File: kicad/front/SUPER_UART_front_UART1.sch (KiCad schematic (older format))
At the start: 46 parts, among them CON1 UART A, CON5 RS232, CON6 UART A, SW16 DTR, SW17 RTS, U1 SN74LVC2T45DCTT, U10 MAX3243EIPW, U13 74HC08N, U14 74HC08N, U2 SN74LVC2T45DCTT

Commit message: Working on schematic
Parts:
- removed C21, C22, C4: 100n, 0603_N, symbol C
- removed C23, C24, C25: 470n, 0603_N, symbol C
- removed CON5: RS232, pnConnector:DB9MV, symbol DB9_MALE
- removed D48: DTR, pnSemiconductor:LED_3.2x2, symbol diode_LED
- removed D49: RTS, pnSemiconductor:LED_3.2x2, symbol diode_LED
- removed MH1, MH2: hole, mounting_hole_3.2_7.5_plated, symbol mounting_hole_plated
- removed R1, R2: R, 0603_R_N, symbol R_V
- removed unit 1 of RN1
- removed RN8: R, 4x0603_N, symbol R_Network_4
- removed SW16: DTR, pnSwitches:TACTB-64K-F, symbol MicroswitchSMT
- removed SW17: RTS, pnSwitches:TACTB-64K-F, symbol MicroswitchSMT
- removed U1, U2: SN74LVC2T45DCTT, niceSemiconductors:TI_SSOP-8_N, symbol SN74LVC2T45DCTT
- removed U10: MAX3243EIPW, TSSOP-28_N, symbol MAX3243EIPW
- removed U13, U14: 74HC08N, DIP-14_N, symbol 74HC08N
- added C13, C26, C28, C31, C34: 100n, 0603_N, symbol C
- added CON4: UART D, pnConnector:NIGINI_NCDW-06, symbol PIN-1x6
- added D21: DTR, pnSemiconductor:LED0603_R, symbol diode_LED
- added D22: CTS, pnSemiconductor:LED0603_R, symbol diode_LED
- added D23: RXD, pnSemiconductor:LED0603_R, symbol diode_LED
- added D24: TXD, pnSemiconductor:LED0603_R, symbol diode_LED
- added D7, D8: PESD5V2S2UT, SOT23-3_N, symbol PESD5V2S2UT
- added Q5, Q6: PDTA143ZT, niceSemiconductors:SOT23-3_N, symbol PDTA143ZT
- added R13, R18: R, 0603_R_N, symbol R_V
- added R14, R15, R16, R17: R, 0603_R_N, symbol R
- added unit 2 of RN1
- added RN3, RN4, RN9: R, pnRLC:4x0603_N, symbol R_network_4
- added T2, T3: DMG1012UW-7, niceSemiconductors:SC70-3_N, symbol N-MOS_small
- added TP6, TP7, TP8, TP9: Testpoint, pnConnector:TP_1mm, symbol Testpoint
- added U1: 74LVC1T45GW, SC70-6_N, symbol 74LVC1T45GW
- added U21, U22: 74LVC8T245PW, TI_TSSOP-24_N, symbol 74LVC8T245PW
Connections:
- net labels added: +3V3, CTS_B, CTS_B_VDDA, CTS_B_VDDB, CTS_D, CTS_D1, CTS_D_VDDA, DCD_D, DCD_D1, DCD_D_VDDA, DSR_D, DSR_D1, DSR_D_VDDA, DTR_B, DTR_B_VDDA, DTR_B_VDDB, DTR_D, DTR_D1, DTR_D_VDDA, I2C_PU_EN_B, I2C_PU_EN_B_VCCA, RI_D, RI_D1, RI_D_VDDA, RTS_D, RTS_D1, RTS_D_VDDA, RXD_B, RXD_B_LED, RXD_B_VDDA, RXD_B_VDDB, RXD_D1, RXD_D_LED, RXD_D_VDDA, TXD_B, TXD_B_LED, TXD_B_VDDA, TXD_B_VDDB, TXD_D, TXD_D_LED, TXD_D_VDDA, VDDA, VDDB, ~CTS_B_OC, ~RXD_B_OC, ~SPI_EN_B
- net labels removed: CTS_A_ISO, CTS_A_LED_ISO, DCD_A_ISO, DCD_A_LED_ISO, DSR_A_ISO, DSR_A_LED_ISO, DTR_A_ISO, DTR_A_LED_ISO, FTDI_DTR_A_ISO, FTDI_DTR_A_ISO1, FTDI_RTS_A_ISO, FTDI_RTS_A_ISO1, FT_CTS_A_ISO, FT_CTS_A_ISO1, FT_CTS_A_ISO2, FT_DCD_A_ISO1, FT_DCD_A_ISO2, FT_DSR_A_ISO1, FT_DSR_A_ISO2, FT_DTR_A_ISO, FT_RI_A_ISO1, FT_RI_A_ISO2, FT_RTS_A_ISO, FT_RXD_A_ISO, FT_RXD_A_ISO1, FT_RXD_A_ISO2, FT_TXD_A_ISO, ISO_3V3, ISO_GND, ISO_VDD, RI_A_ISO, RI_A_LED_ISO, RS_CTS_ISO, RS_DCD_ISO, RS_DSR_ISO, RS_DTR_ISO, RS_RI_ISO, RS_RTS_ISO, RS_RXD_ISO, RS_TXD_ISO, RTS_A_ISO, RTS_A_LED_ISO, RXD_A_ISO, RXD_A_LED, TXD_A_ISO, TXD_A_LED
- wire segments 190 -> 211
- no-connect marks 1 -> 0
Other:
- note added: "Level converter"
- note added: "TTL level connector"
- moved on the sheet: C17, C5, C6, C7, CON1, CON6, D1, D10, D11, D12, D2, D25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

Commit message: Working on schematic
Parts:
- removed D12: CTS, pnSemiconductor:LED0603_R, symbol diode_LED
- removed D29: DSR, pnSemiconductor:LED0603_R, symbol diode_LED
- removed D31: RI, pnSemiconductor:LED0603_R, symbol diode_LED
- removed D32: DCD, pnSemiconductor:LED0603_R, symbol diode_LED
- removed R7: R, 0603_R_N, symbol R
- removed RN4: R, pnRLC:4x0603_N, symbol R_network_4
- removed T2, T3: DMG1012UW-7, niceSemiconductors:SC70-3_N, symbol N-MOS_small
- removed TP6, TP7, TP8, TP9: Testpoint, pnConnector:TP_1mm, symbol Testpoint
- added C26, C32: 100n, 0603_N, symbol C
- added C27: 10n, 0603_N, symbol C
- added C28: 10u, niceRLC:0805_N, symbol C
- added C31: 1u, niceRLC:0603_N, symbol C
- added Q3, Q5: 2N7002PS, niceSemiconductors:SC70-6_N, symbol 2N7002PS
- added Q6: N-MOS_small, SOT23-3_N, symbol N-MOS_small
- added R14: R, 0603_R_N, symbol R
- added R15, R18, R19, R21, R22, R26: 10k, 0603_R_N, symbol R_V
- added R20: 4k7, 0603_R_N, symbol R_V
- added R23: 1k8, 0603_R_N, symbol R_V
- added R24: 3k9, 0603_R_N, symbol R_V
- added R25: 6k8, 0603_R_N, symbol R_V
- added R27: 5k6, 0603_R_N, symbol R
- added R28: 47k, 0603_R_N, symbol R
- added U10: LP2951CD, SOIC-8_N, symbol LP2951CD
- LED29: renamed from D9; Fieldname (none) -> Value
- renumbered C17 to C19, C28 to C20, C5 to C21, C34 to C22, C13 to C23, C31 to C24, C26 to C25, C6 to C29, C7 to C30, CON6 to CON4, CON1 to CON5, CON4 to CON6, D25 to D2, D26 to D3, D27 to D4, D28 to D5, D1 to D6, D2 to D7, D7 to D8, D8 to D9, D11 to LED27, D10 to LED28, D30 to LED30, D21 to LED31, D22 to LED32, D23 to LED33, D24 to LED34, Q5 to Q2, Q6 to Q4, R13 to R10, R15 to R11, R16 to R12, R8 to R13, R18 to R16, R9 to R7, R10 to R8, R14 to R9, RN1 to RN4, RN9 to RN5, RN3 to RN6, U21 to U7, U22 to U8, U1 to U9
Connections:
- net labels added: +5V, CTS_B_VDD1, CTS_D_VDD1, DCD_D_VDD1, DSR_D_VDD1, DTR_B_VDD1, DTR_D_VDD1, RI_D_VDD1, RTS_D_VDD1, RXD_B_VDD1, RXD_D_VDD1, SPI_EN_B, TXD_B_VDD1, TXD_D_VDD1, VDD1, VDD1_SEL1, VDD1_SEL2, VDD1_SEL3, ~VDD1_EN, ~VDD1_ERR
- net labels removed: CTS_B_VDDA, CTS_B_VDDB, CTS_D, CTS_D_VDDA, DCD_D, DCD_D_VDDA, DSR_D, DSR_D_VDDA, DTR_B_VDDA, DTR_B_VDDB, DTR_D, DTR_D_VDDA, RI_D, RI_D_VDDA, RTS_D, RTS_D_VDDA, RXD_B_VDDA, RXD_B_VDDB, RXD_D_VDDA, TXD_B_VDDA, TXD_B_VDDB, TXD_D_VDDA, VDDA, VDDB, ~SPI_EN_B
- wire segments 211 -> 241
- no-connect marks 0 -> 6
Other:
- note removed: "Level converter"
- note removed: "TTL level connector"
- moved on the sheet: C19, C20, C21, C22, C23, C24, C25, C29, C30, CON4, CON5, CON6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

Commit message: Working on schematic
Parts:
- CON4, CON5: value UART A -> PORT D
- CON6: value UART D -> PORT B
- LED27, LED28, LED29, LED30, LED31, LED32, LED33, LED34: footprint pnSemiconductor:LED0603_R -> pnSemiconductor:0805D

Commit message: PCB placement
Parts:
- removed Q3: 2N7002PS, niceSemiconductors:SC70-6_N, symbol 2N7002PS
- added Q3, Q8: N-MOS_small, SOT23-3_N, symbol N-MOS_small
- RN4, RN5, RN6: footprint pnRLC:4x0603_N -> niceRLC:4x0603_N
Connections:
- net CTS_B_VDD1: now also Q8.3 (D)
- net CTS_D_VDD1: now also RN5.3; no longer RN5.2
- net DCD_D_VDD1: now also RN5.2; no longer RN5.3
- net DSR_D_VDD1: now also RN5.1; no longer RN5.4
- net DTR_D_VDD1: now also RN4.3; no longer RN4.2
- net GND: now also Q3.2 (S), Q8.2 (S)
- net RTS_D_VDD1: now also RN4.2; no longer RN4.3
- net RXD_B_VDD1: now also Q3.3 (D)
- net RXD_D_VDD1: now also RN5.4; no longer RN5.1
- net TXD_B_VDD1: now also RN4.1; no longer RN4.4
- net TXD_D_VDD1: now also RN4.4; no longer RN4.1
- net VDD1_SEL1: now also Q6.1 (G); no longer Q5.1 (G)
- net VDD1_SEL3: now also Q5.1 (G); no longer Q6.1 (G)
- net ~CTS_B_OC: now also Q8.1 (G)
- net ~RXD_B_OC: now also Q3.1 (G)
- net at RN4.8: now also U7.18 (B4); no longer U7.21 (B1)
- net at RN4.5: now also U7.21 (B1); no longer U7.18 (B4)
- net at U7.19 (B3): now also RN4.7; no longer RN4.6
- net at U7.20 (B2): now also RN4.6; no longer RN4.7
- net at U8.18 (B4): now also RN5.8; no longer RN5.5
- net at U8.19 (B3): now also RN5.7; no longer RN5.6
- net at U8.20 (B2): now also RN5.6; no longer RN5.7
- net at U8.21 (B1): now also RN5.5; no longer RN5.8
- net at C32.1, R23.1, R28.2: now also Q6.3 (D); no longer Q5.6 (D)
- net at R25.1: now also Q5.6 (D); no longer Q6.3 (D)
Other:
- moved on the sheet: Q5A, Q6, RN4A, RN4B, RN4C, RN4D, RN5A, RN5B, RN5C, RN5D

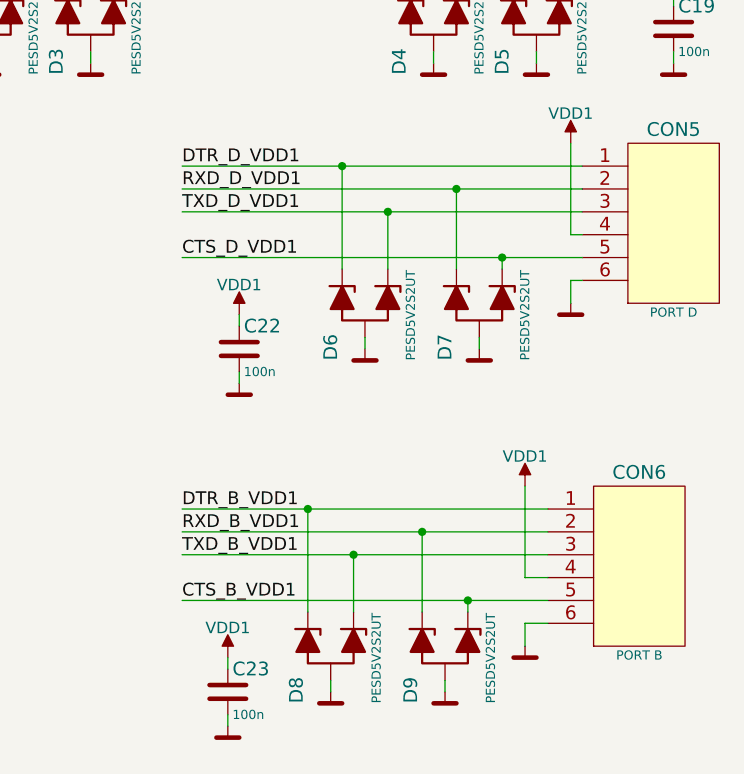
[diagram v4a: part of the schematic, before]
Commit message: Routing before moving to 4 layers
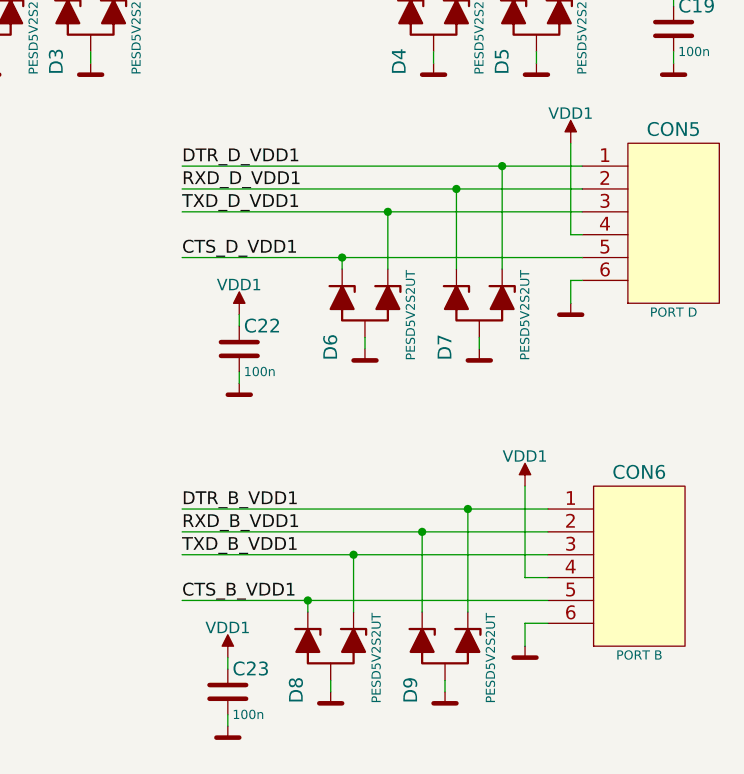
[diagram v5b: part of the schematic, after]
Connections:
- net CTS_B_VDD1: now also D8.1 (C1); no longer D9.2 (C2)
- net CTS_D_VDD1: now also D6.1 (C1); no longer D7.2 (C2)
- net DTR_B_VDD1: now also D9.2 (C2); no longer D8.1 (C1)
- net DTR_D_VDD1: now also D7.2 (C2); no longer D6.1 (C1)

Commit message: Front board routed
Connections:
- net DCD_D1: now also U8.6 (A4); no longer U8.5 (A3)
- net DCD_D_VDD1: now also RN5.1; no longer RN5.2
- net DSR_D1: now also U8.5 (A3); no longer U8.6 (A4)
- net DSR_D_VDD1: now also RN5.2; no longer RN5.1
- net RXD_B_LED: now also RN6.6; no longer RN6.7
- net TXD_B_LED: now also RN6.7; no longer RN6.6
- net at LED33.2 (C): now also RN6.2; no longer RN6.3
- net at LED34.2 (C): now also RN6.3; no longer RN6.2

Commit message: Add missing files
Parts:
- Q5: value 2N7002PS -> N.C.
- Q6: value N-MOS_small -> N.C.
- R10: value R -> 4k7
- R11, R12, R17, RN4, RN5: value R -> 100R
- R13, R14, R7, R8, RN6: value R -> 1k
- R16: value R -> 4k7; Fieldname (none) -> Value
- R20: value 4k7 -> 100k
- R23: value 1k8 -> 47k
- R24: value 3k9 -> N.C.
- R25: value 6k8 -> N.C.
- R26: value 10k -> 47k
- R9, RN4, RN5: value R -> 100R; Fieldname (none) -> Value
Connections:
- net I2C_PU_EN_B_VCCA: no longer Q2.1 (B), U7.16 (B6)
- net I2C_PU_EN_B renamed ~I2C_PU_EN_B
- new net ~I2C_PU_EN_B_VCCA: Q2.1 (B), U7.16 (B6)
